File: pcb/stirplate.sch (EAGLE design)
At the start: 18 parts, among them IC1 ATMEGA168-PU, IC2 7805T, T1 2N2222, X1 HD44780LCD-1602

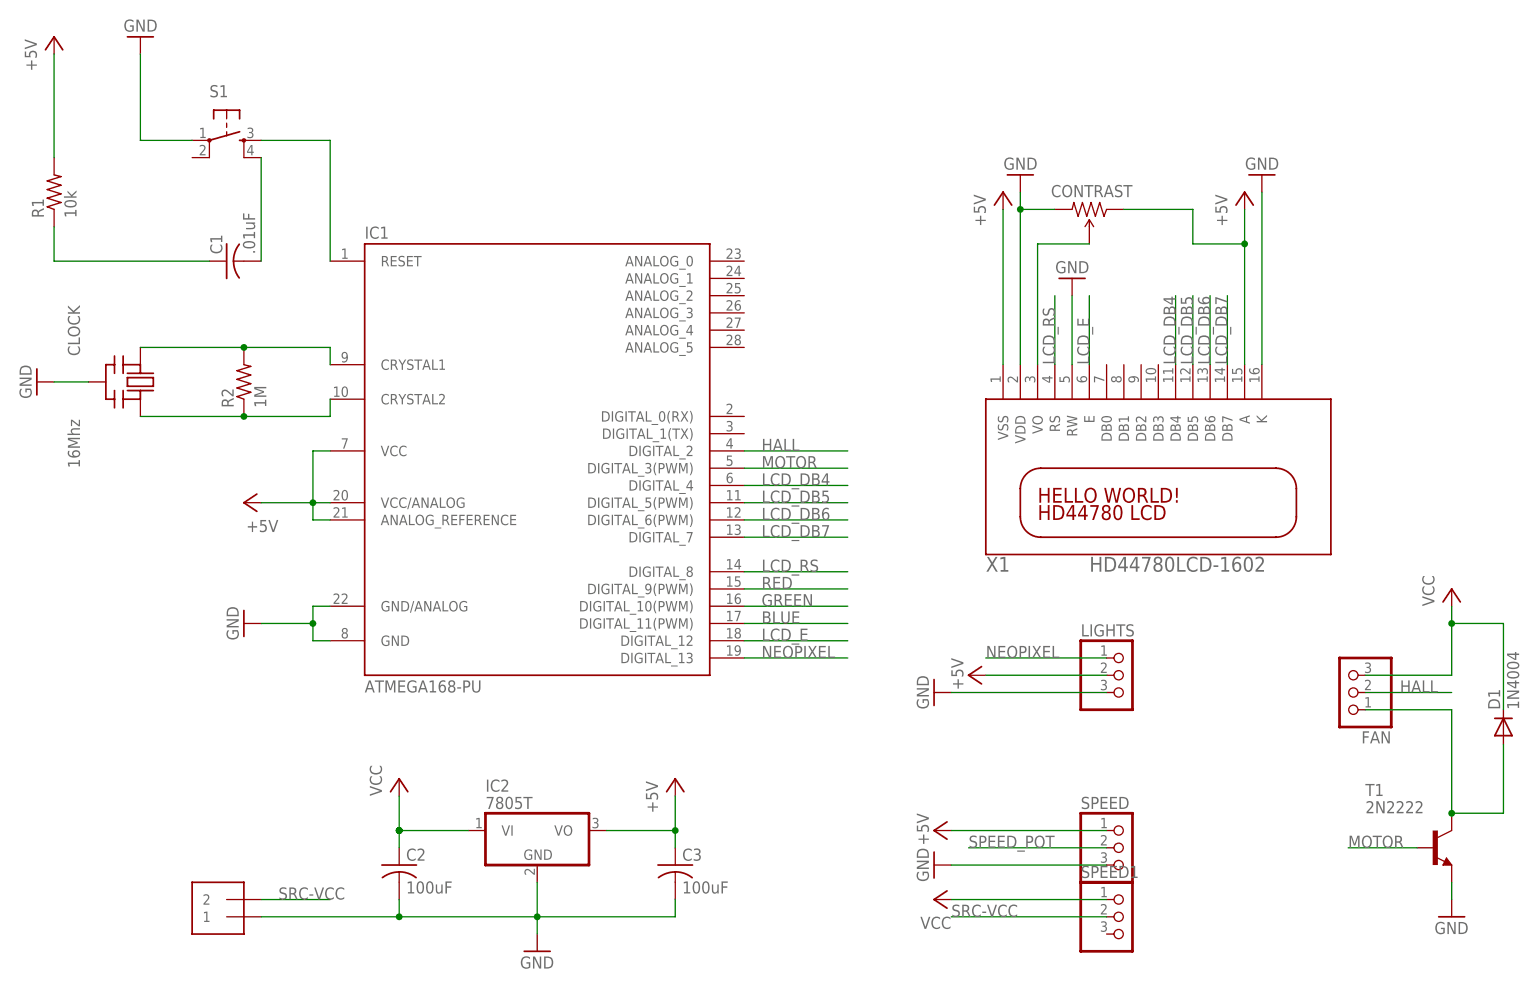
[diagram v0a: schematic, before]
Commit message: Fixed a few issues on the new eagle board
Upgraded LCD to an Adafruit RGB, fixed some routing caused by that.
Moved header for radial pot to a 1x5 screw terminal and fixed routing on
that.
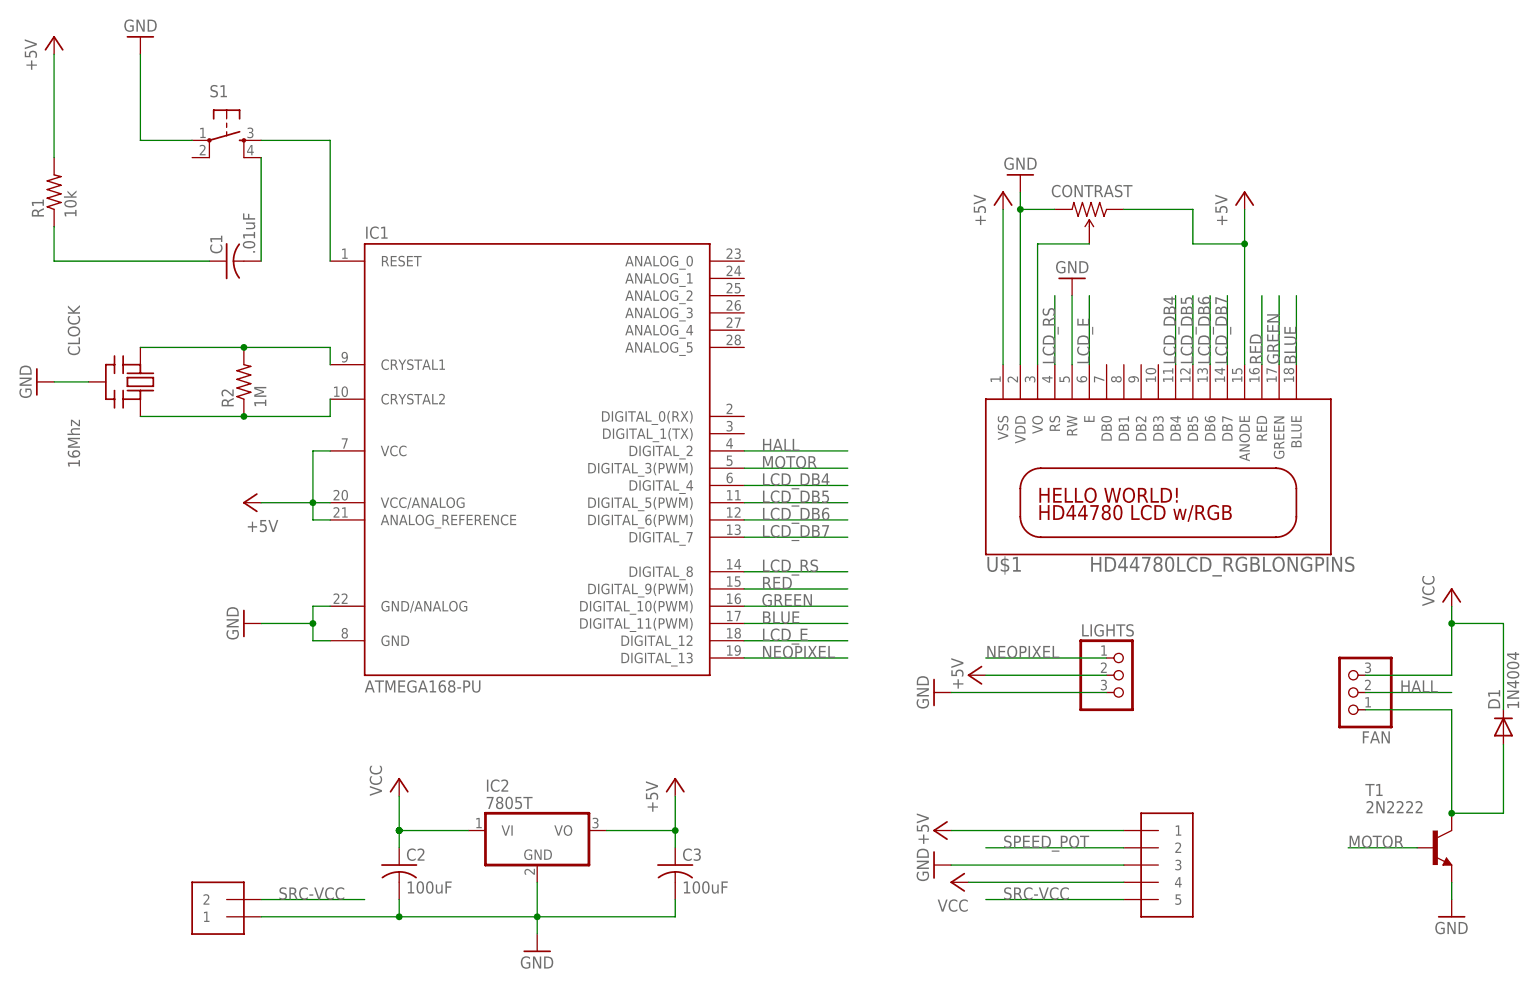
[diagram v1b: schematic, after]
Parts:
- removed SPEED1: (no value), adafruit:PINHD-1X3
- removed X1: HD44780LCD-1602, adafruit:HD44780LCD-1602
- added U$1: HD44780LCD_RGBLONGPINS, adafruit:HD44780LCD_RGBLONGPINS
- SPEED: value (none) -> 1X5; device adafruit:PINHD-1X3 -> adafruit:1X5
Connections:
- new net VDD: CONTRAST.CW, U$1.VDD
- new net VSS: U$1.VSS
- net +5V: now also U$1.ANODE; no longer X1.A, X1.VSS
- net BLUE: now also U$1.BLUE
- net GND: now also U$1.RW; no longer CONTRAST.CW, X1.K, X1.RW, X1.VDD
- net GREEN: now also U$1.GREEN
- net LCD_DB4: now also U$1.DB4; no longer X1.DB4
- net LCD_DB5: now also U$1.DB5; no longer X1.DB5
- net LCD_DB6: now also U$1.DB6; no longer X1.DB6
- net LCD_DB7: now also U$1.DB7; no longer X1.DB7
- net LCD_E: now also U$1.E; no longer X1.E
- net LCD_RS: now also U$1.RS; no longer X1.RS
- net N$7: now also U$1.VO; no longer X1.VO
- net RED: now also U$1.RED
- net SRC-VCC: now also SPEED.5; no longer SPEED1.2
- net VCC: now also SPEED.4; no longer SPEED1.1
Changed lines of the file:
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@@
 <part name="R1" library="adafruit" deviceset="R-US_" device="0204/7" value="10k"/>
 <part name="P+4" library="supply1" deviceset="+5V" device=""/>
-<part name="X1" library="adafruit" deviceset="HD44780LCD" device="-1602"/>
 <part name="T1" library="adafruit" deviceset="2N2222" device=""/>
-<part name="SPEED" library="adafruit" deviceset="PINHD-1X3" device=""/>
 <part name="GND5" library="supply1" deviceset="GND" device=""/>
 <part name="P+6" library="supply1" deviceset="+5V" device=""/>
@@
 <part name="CONTRAST" library="SparkFun-Electromechanical" deviceset="TRIMPOT" device="PTH"/>
 <part name="P+8" library="supply1" deviceset="+5V" device=""/>
-<part name="GND8" library="supply1" deviceset="GND" device=""/>
 <part name="GND9" library="supply1" deviceset="GND" device=""/>
-<part name="SPEED1" library="adafruit" deviceset="PINHD-1X3" device=""/>
 <part name="P+9" library="supply1" deviceset="VCC" device=""/>
 <part name="LIGHTS" library="adafruit" deviceset="PINHD-1X3" device=""/>
 <part name="P+10" library="supply1" deviceset="+5V" device=""/>
 <part name="GND10" library="supply1" deviceset="GND" device=""/>
+<part name="SPEED" library="adafruit" deviceset="1X5" device=""/>
+<part name="U$1" library="adafruit" deviceset="HD44780LCD_RGB" device="LONGPINS"/>
 </parts>
 <sheets>
@@
 <instance part="R1" gate="G$1" x="-5.08" y="116.84" rot="R90"/>
 <instance part="P+4" gate="1" x="-5.08" y="139.7"/>
-<instance part="X1" gate="G$1" x="157.48" y="73.66"/>
 <instance part="T1" gate="G$1" x="198.12" y="20.32"/>
-<instance part="SPEED" gate="A" x="152.4" y="20.32"/>
 <instance part="GND5" gate="1" x="124.46" y="17.78" rot="R270"/>
 <instance part="P+6" gate="1" x="124.46" y="22.86" smashed="yes" rot="R90">
@@
 </instance>
 <instance part="P+8" gate="1" x="170.18" y="116.84"/>
-<instance part="GND8" gate="1" x="172.72" y="119.38" rot="R180"/>
 <instance part="GND9" gate="1" x="144.78" y="104.14" rot="R180"/>
-<instance part="SPEED1" gate="A" x="152.4" y="10.16"/>
-<instance part="P+9" gate="VCC" x="124.46" y="12.7" rot="R90"/>
+<instance part="P+9" gate="VCC" x="127" y="15.24" rot="R90"/>
 <instance part="LIGHTS" gate="A" x="152.4" y="45.72"/>
 <instance part="P+10" gate="1" x="129.54" y="45.72" smashed="yes" rot="R90">
@@
 </instance>
 <instance part="GND10" gate="1" x="124.46" y="43.18" rot="R270"/>
+<instance part="SPEED" gate="G$1" x="160.02" y="17.78"/>
+<instance part="U$1" gate="G$1" x="157.48" y="73.66"/>
 </instances>
 <busses>
@@
 </segment>
 <segment>
-<pinref part="SPEED" gate="A" pin="3"/>
 <pinref part="GND5" gate="1" pin="GND"/>
-<wire x1="149.86" y1="17.78" x2="127" y2="17.78" width="0.1524" layer="91"/>
+<wire x1="152.4" y1="17.78" x2="127" y2="17.78" width="0.1524" layer="91"/>
+<pinref part="SPEED" gate="G$1" pin="3"/>
 </segment>
 <segment>
@@
 </segment>
 <segment>
-<pinref part="X1" gate="G$1" pin="VDD"/>
-<pinref part="GND7" gate="1" pin="GND"/>
-<wire x1="137.16" y1="116.84" x2="137.16" y2="114.3" width="0.1524" layer="91"/>
-<pinref part="CONTRAST" gate="R?" pin="CW"/>
-<wire x1="137.16" y1="114.3" x2="137.16" y2="91.44" width="0.1524" layer="91"/>
-<wire x1="142.24" y1="114.3" x2="137.16" y2="114.3" width="0.1524" layer="91"/>
-<junction x="137.16" y="114.3"/>
-</segment>
-<segment>
-<pinref part="X1" gate="G$1" pin="K"/>
-<pinref part="GND8" gate="1" pin="GND"/>
-<wire x1="172.72" y1="116.84" x2="172.72" y2="91.44" width="0.1524" layer="91"/>
-</segment>
-<segment>
-<pinref part="X1" gate="G$1" pin="RW"/>
 <wire x1="144.78" y1="91.44" x2="144.78" y2="101.6" width="0.1524" layer="91"/>
 <pinref part="GND9" gate="1" pin="GND"/>
+<pinref part="U$1" gate="G$1" pin="RW"/>
 </segment>
 <segment>
@@
 </segment>
 </net>
-<net name="+5V" class="0">
+<net name="+5V" class="1">
 <segment>
 <pinref part="IC2" gate="A1" pin="VO"/>
@@
 </segment>
 <segment>
-<pinref part="SPEED" gate="A" pin="1"/>
 <pinref part="P+6" gate="1" pin="+5V"/>
-<wire x1="149.86" y1="22.86" x2="127" y2="22.86" width="0.1524" layer="91"/>
-</segment>
-<segment>
-<pinref part="X1" gate="G$1" pin="VSS"/>
-<wire x1="134.62" y1="91.44" x2="134.62" y2="114.3" width="0.1524" layer="91"/>
-<pinref part="P+5" gate="1" pin="+5V"/>
-</segment>
-<segment>
-<pinref part="X1" gate="G$1" pin="A"/>
+<wire x1="152.4" y1="22.86" x2="127" y2="22.86" width="0.1524" layer="91"/>
+<pinref part="SPEED" gate="G$1" pin="1"/>
+</segment>
+<segment>
 <wire x1="170.18" y1="91.44" x2="170.18" y2="109.22" width="0.1524" layer="91"/>
 <pinref part="P+8" gate="1" pin="+5V"/>
@@
 <wire x1="162.56" y1="109.22" x2="170.18" y2="109.22" width="0.1524" layer="91"/>
 <junction x="170.18" y="109.22"/>
+<pinref part="U$1" gate="G$1" pin="ANODE"/>
 </segment>
 <segment>
@@
 </segment>
 <segment>
-<pinref part="SPEED1" gate="A" pin="1"/>
-<wire x1="149.86" y1="12.7" x2="127" y2="12.7" width="0.1524" layer="91"/>
+<wire x1="152.4" y1="15.24" x2="129.54" y2="15.24" width="0.1524" layer="91"/>
 <pinref part="P+9" gate="VCC" pin="VCC"/>
+<pinref part="SPEED" gate="G$1" pin="4"/>
 </segment>
 </net>
@@
 <net name="SPEED_POT" class="0">
 <segment>
-<pinref part="SPEED" gate="A" pin="2"/>
-<wire x1="149.86" y1="20.32" x2="129.54" y2="20.32" width="0.1524" layer="91"/>
-<label x="129.54" y="20.32" size="1.778" layer="95"/>
+<wire x1="152.4" y1="20.32" x2="132.08" y2="20.32" width="0.1524" layer="91"/>
+<label x="134.62" y="20.32" size="1.778" layer="95"/>
+<pinref part="SPEED" gate="G$1" pin="2"/>
 </segment>
 </net>
 <net name="N$7" class="0">
 <segment>
-<pinref part="X1" gate="G$1" pin="VO"/>
 <wire x1="139.7" y1="91.44" x2="139.7" y2="109.22" width="0.1524" layer="91"/>
 <wire x1="139.7" y1="109.22" x2="147.32" y2="109.22" width="0.1524" layer="91"/>
 <pinref part="CONTRAST" gate="R?" pin="WIPER"/>
+<pinref part="U$1" gate="G$1" pin="VO"/>
 </segment>
 </net>
 <net name="LCD_RS" class="0">
 <segment>
-<pinref part="X1" gate="G$1" pin="RS"/>
 <wire x1="142.24" y1="91.44" x2="142.24" y2="101.6" width="0.1524" layer="91"/>
 <label x="142.24" y="91.44" size="1.778" layer="95" rot="R90"/>
+<pinref part="U$1" gate="G$1" pin="RS"/>
 </segment>
 <segment>
@@
 <net name="LCD_E" class="0">
 <segment>
-<pinref part="X1" gate="G$1" pin="E"/>
 <wire x1="147.32" y1="91.44" x2="147.32" y2="101.6" width="0.1524" layer="91"/>
 <label x="147.32" y="91.44" size="1.778" layer="95" rot="R90"/>
+<pinref part="U$1" gate="G$1" pin="E"/>
 </segment>
 <segment>
@@
 <net name="LCD_DB7" class="0">
 <segment>
-<pinref part="X1" gate="G$1" pin="DB7"/>
 <wire x1="167.64" y1="91.44" x2="167.64" y2="101.6" width="0.1524" layer="91"/>
 <label x="167.64" y="91.44" size="1.778" layer="95" rot="R90"/>
+<pinref part="U$1" gate="G$1" pin="DB7"/>
 </segment>
 <segment>
@@
 <net name="LCD_DB6" class="0">
 <segment>
-<pinref part="X1" gate="G$1" pin="DB6"/>
 <wire x1="165.1" y1="91.44" x2="165.1" y2="101.6" width="0.1524" layer="91"/>
 <label x="165.1" y="91.44" size="1.778" layer="95" rot="R90"/>
+<pinref part="U$1" gate="G$1" pin="DB6"/>
 </segment>
 <segment>
@@
 <net name="LCD_DB5" class="0">
 <segment>
-<pinref part="X1" gate="G$1" pin="DB5"/>
 <wire x1="162.56" y1="91.44" x2="162.56" y2="101.6" width="0.1524" layer="91"/>
 <label x="162.56" y="91.44" size="1.778" layer="95" rot="R90"/>
+<pinref part="U$1" gate="G$1" pin="DB5"/>
 </segment>
 <segment>
@@
 <net name="LCD_DB4" class="0">
 <segment>
-<pinref part="X1" gate="G$1" pin="DB4"/>
 <wire x1="160.02" y1="91.44" x2="160.02" y2="101.6" width="0.1524" layer="91"/>
 <label x="160.02" y="91.44" size="1.778" layer="95" rot="R90"/>
+<pinref part="U$1" gate="G$1" pin="DB4"/>
 </segment>
 <segment>
@@
 <label x="99.06" y="58.42" size="1.778" layer="95"/>
 </segment>
+<segment>
+<wire x1="172.72" y1="101.6" x2="172.72" y2="91.44" width="0.1524" layer="91"/>
+<pinref part="U$1" gate="G$1" pin="RED"/>
+<label x="172.72" y="91.44" size="1.778" layer="95" rot="R90"/>
+</segment>
 </net>
 <net name="GREEN" class="0">
@@
 <label x="99.06" y="55.88" size="1.778" layer="95"/>
 </segment>
+<segment>
+<pinref part="U$1" gate="G$1" pin="GREEN"/>
+<wire x1="175.26" y1="91.44" x2="175.26" y2="101.6" width="0.1524" layer="91"/>
+<label x="175.26" y="91.44" size="1.778" layer="95" rot="R90"/>
+</segment>
 </net>
 <net name="BLUE" class="0">
@@
 <label x="99.06" y="53.34" size="1.778" layer="95"/>
 </segment>
+<segment>
+<pinref part="U$1" gate="G$1" pin="BLUE"/>
+<wire x1="177.8" y1="91.44" x2="177.8" y2="101.6" width="0.1524" layer="91"/>
+<label x="177.8" y="91.44" size="1.778" layer="95" rot="R90"/>
+</segment>
 </net>
 <net name="SRC-VCC" class="1">
 <segment>
 <pinref part="POWER" gate="G$1" pin="2"/>
-<wire x1="25.4" y1="12.7" x2="35.56" y2="12.7" width="0.1524" layer="91"/>
+<wire x1="25.4" y1="12.7" x2="40.64" y2="12.7" width="0.1524" layer="91"/>
 <label x="27.94" y="12.7" size="1.778" layer="95"/>
 </segment>
 <segment>
-<pinref part="SPEED1" gate="A" pin="2"/>
-<wire x1="149.86" y1="10.16" x2="127" y2="10.16" width="0.1524" layer="91"/>
-<label x="127" y="10.16" size="1.778" layer="95"/>
+<wire x1="152.4" y1="12.7" x2="132.08" y2="12.7" width="0.1524" layer="91"/>
+<label x="134.62" y="12.7" size="1.778" layer="95"/>
+<pinref part="SPEED" gate="G$1" pin="5"/>
 </segment>
 </net>
@@
 </segment>
 </net>
+<net name="VDD" class="1">
+<segment>
+<pinref part="GND7" gate="1" pin="GND"/>
+<wire x1="137.16" y1="116.84" x2="137.16" y2="114.3" width="0.1524" layer="91"/>
+<pinref part="CONTRAST" gate="R?" pin="CW"/>
+<wire x1="137.16" y1="114.3" x2="137.16" y2="91.44" width="0.1524" layer="91"/>
+<wire x1="142.24" y1="114.3" x2="137.16" y2="114.3" width="0.1524" layer="91"/>
+<junction x="137.16" y="114.3"/>
+<pinref part="U$1" gate="G$1" pin="VDD"/>
+</segment>
+</net>
+<net name="VSS" class="1">
+<segment>
+<wire x1="134.62" y1="91.44" x2="134.62" y2="114.3" width="0.1524" layer="91"/>
+<pinref part="P+5" gate="1" pin="+5V"/>
+<pinref part="U$1" gate="G$1" pin="VSS"/>
+</segment>
+</net>
